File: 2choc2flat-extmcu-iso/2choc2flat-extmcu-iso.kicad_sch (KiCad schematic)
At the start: 136 parts, among them J1 Conn_01x09_Male, J2 Conn_01x05_Male, J3 Conn_01x09_Male, K1 KEYSW, K10 KEYSW, K11 KEYSW, K12 KEYSW, K13 KEYSW, K14 KEYSW, K15-1 KEYSW, K16 KEYSW, K17 KEYSW, K18 KEYSW, K19 KEYSW, K2 KEYSW, K20 KEYSW, K21 KEYSW, K22 KEYSW, K23 KEYSW, K24 KEYSW, K25 KEYSW, K26 KEYSW, K27 KEYSW, K28 KEYSW, K3 KEYSW, K31 KEYSW, K31-1 KEYSW, K32 KEYSW, K33 KEYSW, K34 KEYSW, K35 KEYSW, K36 KEYSW, K37 KEYSW, K38 KEYSW, K39 KEYSW, K4 KEYSW, K40 KEYSW, K41 KEYSW, K42 KEYSW, K43 KEYSW, K44 KEYSW, K46 KEYSW, K48 KEYSW, K49 KEYSW, K5 KEYSW, K50 KEYSW, K51 KEYSW, K52 KEYSW, K53 KEYSW, K54 KEYSW, K55 KEYSW, K56 KEYSW, K57 KEYSW, K58 KEYSW, K59 KEYSW, K6 KEYSW, K61 KEYSW, K62 KEYSW, K63 KEYSW, K67 KEYSW, K7 KEYSW, K71 KEYSW, K72 KEYSW, K73 KEYSW, K74 KEYSW, K8 KEYSW, K9 KEYSW

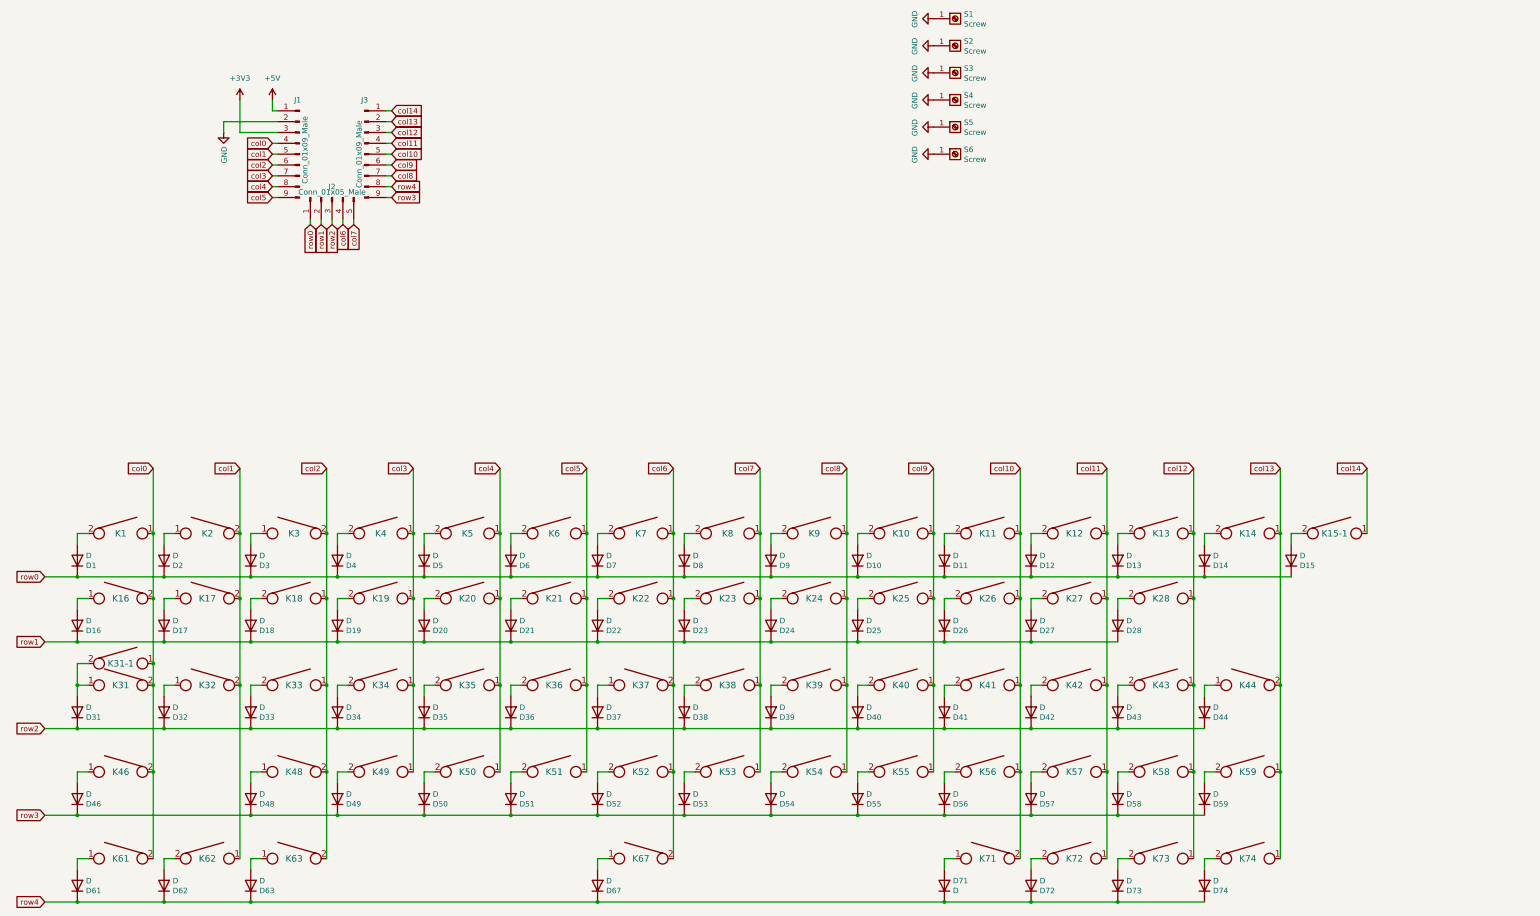
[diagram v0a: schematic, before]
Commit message: make ISO 64 2u left shift layout
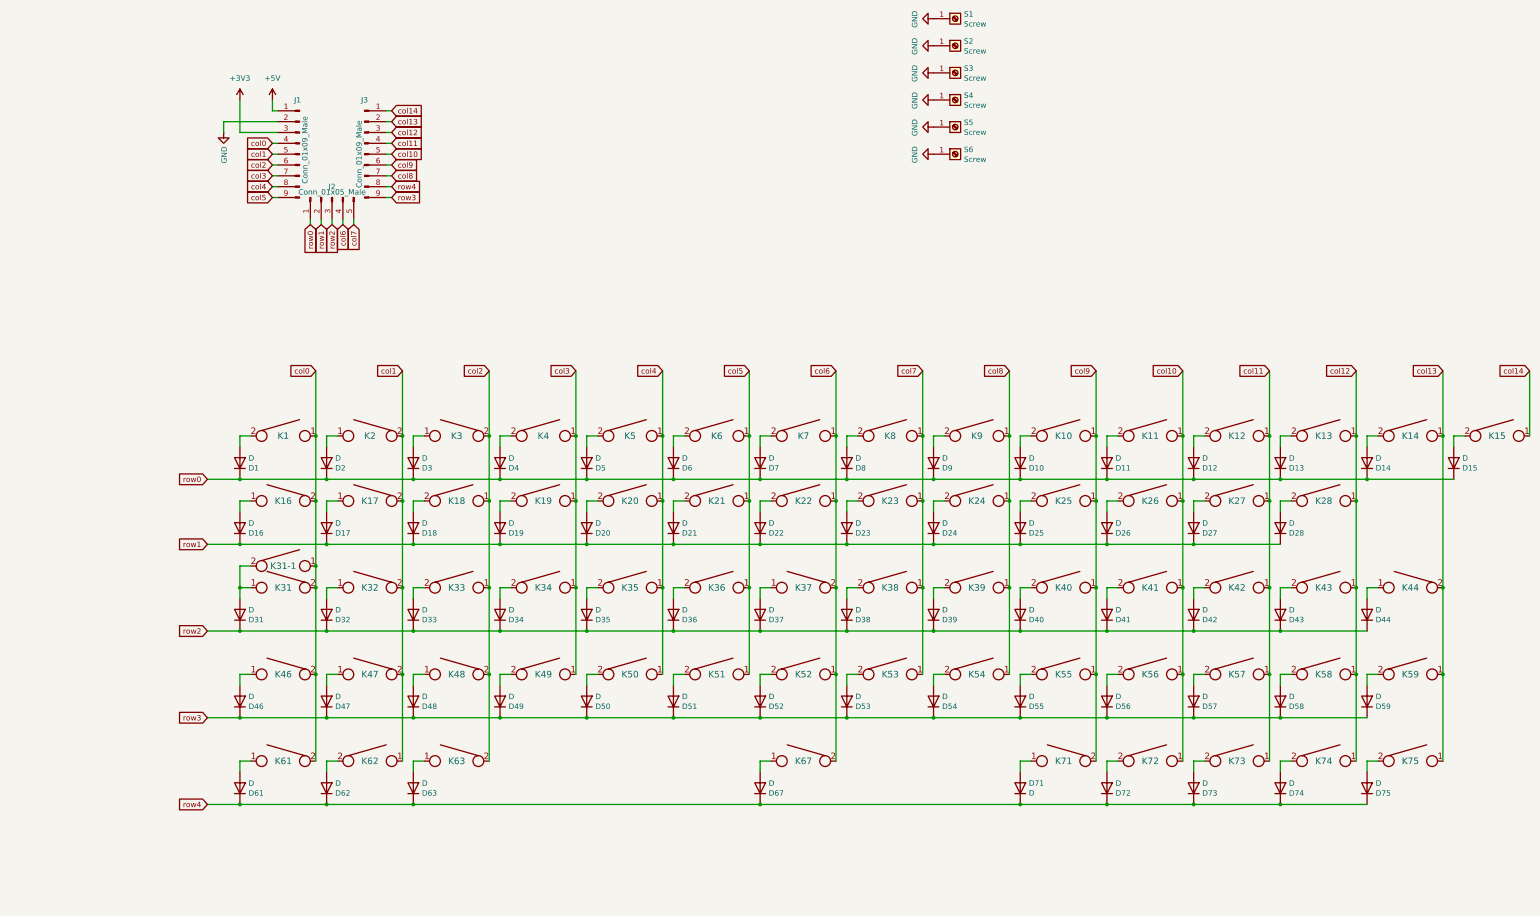
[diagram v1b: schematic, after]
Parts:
- removed K15-1: KEYSW, Switch_Keyboard_Hotswap_Kailh_mine:SW_Hotswap_Kailh_Choc_V2_1.00u, symbol keyboard_parts:KEYSW
- added D47, D75: D, Diode_SMD:D_0805_2012Metric, symbol Device:D
- added K15, K47, K75: KEYSW, Switch_Keyboard_Hotswap_Kailh_mine:SW_Hotswap_Kailh_Choc_V2_1.00u, symbol keyboard_parts:KEYSW
- K46: footprint Switch_Keyboard_Hotswap_Kailh_mine:SW_Hotswap_Kailh_Choc_V2_2.25u_90deg_Gateron_LP_Stabs -> Switch_Keyboard_Hotswap_Kailh_mine:SW_Hotswap_Kailh_Choc_V2_2.00u_90deg_Gateron_LP_Stabs
- K58: footprint Switch_Keyboard_Hotswap_Kailh_mine:SW_Hotswap_Kailh_Choc_V2_1.75u -> Switch_Keyboard_Hotswap_Kailh_mine:SW_Hotswap_Kailh_Choc_V2_1.00u
- K71, K72, K73, K74: footprint Switch_Keyboard_Hotswap_Kailh_mine:SW_Hotswap_Kailh_Choc_V2_1.25u -> Switch_Keyboard_Hotswap_Kailh_mine:SW_Hotswap_Kailh_Choc_V2_1.00u
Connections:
- net col1: now also K47.2
- net col10: now also K72.1; no longer K71.2
- net col11: now also K73.1; no longer K72.1
- net col12: now also K74.1; no longer K73.1
- net col13: now also K75.1; no longer K74.1
- net col14: now also K15.1
- net col9: now also K71.2
- net row3: now also D47.1 (K)
- net row4: now also D75.1 (K)
- net at D15.2 (A): now also K15.2
- new net: D75.2 (A), K75.2
- new net: D47.2 (A), K47.1
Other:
- moved on the sheet: D1, D10, D11, D12, D13, D14, D16, D17, D18, D19, D2, D20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

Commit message: rejigger stabs to work with plates
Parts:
- K67: footprint Switch_Keyboard_Hotswap_Kailh_mine:SW_Hotswap_Kailh_Choc_V2_6.25u_LP_Gateron_Stabs -> Switch_Keyboard_Hotswap_Kailh_mine:SW_Hotswap_Kailh_Choc_V2_6.25u
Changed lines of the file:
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@@
   (junction (at 125.73 158.75) (diameter 0) (color 0 0 0 0)
   )
-  (junction (at 207.01 179.07) (diameter 0) (color 0 0 0 0)
-  )
   (junction (at 85.09 138.43) (diameter 0) (color 0 0 0 0)
   )
@@
   (junction (at 308.61 123.19) (diameter 0) (color 0 0 0 0)
   )
+  (junction (at 207.01 179.07) (diameter 0) (color 0 0 0 0)
+  )
   (junction (at 107.95 133.35) (diameter 0) (color 0 0 0 0)
   )
@@
     (stroke (width 0) (type default) (color 0 0 0 0))
   )
+  (wire (pts (xy 207.01 179.07) (xy 207.01 199.39))
+    (stroke (width 0) (type default) (color 0 0 0 0))
+  )
   (wire (pts (xy 85.09 123.19) (xy 85.09 138.43))
     (stroke (width 0) (type default) (color 0 0 0 0))
@@
     (stroke (width 0) (type default) (color 0 0 0 0))
   )
+  (wire (pts (xy 189.23 199.39) (xy 189.23 201.93))
+    (stroke (width 0) (type default) (color 0 0 0 0))
+  )
   (wire (pts (xy 148.59 140.97) (xy 148.59 138.43))
     (stroke (width 0) (type default) (color 0 0 0 0))
@@
     (stroke (width 0) (type default) (color 0 0 0 0))
   )
+  (wire (pts (xy 191.77 199.39) (xy 189.23 199.39))
+    (stroke (width 0) (type default) (color 0 0 0 0))
+  )
   (wire (pts (xy 351.79 125.73) (xy 351.79 123.19))
     (stroke (width 0) (type default) (color 0 0 0 0))
@@
     (stroke (width 0) (type default) (color 0 0 0 0))
   )
-  (wire (pts (xy 189.23 199.39) (xy 191.77 199.39))
-    (stroke (width 0) (type default) (color 0 0 0 0))
-  )
   (wire (pts (xy 128.27 161.29) (xy 128.27 158.75))
     (stroke (width 0) (type default) (color 0 0 0 0))
@@
     (stroke (width 0) (type default) (color 0 0 0 0))
   )
-  (wire (pts (xy 189.23 201.93) (xy 189.23 199.39))
-    (stroke (width 0) (type default) (color 0 0 0 0))
-  )
   (wire (pts (xy 189.23 148.59) (xy 209.55 148.59))
     (stroke (width 0) (type default) (color 0 0 0 0))
@@
     (stroke (width 0) (type default) (color 0 0 0 0))
   )
-  (wire (pts (xy 207.01 179.07) (xy 207.01 199.39))
-    (stroke (width 0) (type default) (color 0 0 0 0))
-  )
   (wire (pts (xy 166.37 179.07) (xy 166.37 158.75))
     (stroke (width 0) (type default) (color 0 0 0 0))
@@
       (effects (font (size 1.524 1.524)) hide)
     )
-    (property "Footprint" "Switch_Keyboard_Hotswap_Kailh_mine:SW_Hotswap_Kailh_Choc_V2_6.25u_LP_Gateron_Stabs" (id 2) (at 199.39 199.39 0)
+    (property "Footprint" "Switch_Keyboard_Hotswap_Kailh_mine:SW_Hotswap_Kailh_Choc_V2_6.25u" (id 2) (at 199.39 199.39 0)
       (effects (font (size 1.524 1.524)) hide)
     )
@@
     )
     (path "/00000000-0000-0000-0000-00005c555e38"
-      (reference "K67") (unit 1) (value "KEYSW") (footprint "Switch_Keyboard_Hotswap_Kailh_mine:SW_Hotswap_Kailh_Choc_V2_6.25u_LP_Gateron_Stabs")
+      (reference "K67") (unit 1) (value "KEYSW") (footprint "Switch_Keyboard_Hotswap_Kailh_mine:SW_Hotswap_Kailh_Choc_V2_6.25u")
     )
     (path "/00000000-0000-0000-0000-00005cb7e685"

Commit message: relayout using MCU with FFC USB
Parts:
- added LD1: LED, LED_SMD:LED_1206_3216Metric_ReverseMount_Hole1.8x2.4mm, symbol Device:LED
- added R1: R_Small_US, Resistor_SMD:R_0603_1608Metric, symbol Device:R_Small_US
- D1, D10, D11, D12, D13, D14, D15, D16, D17, D18, D19, D2, D20, D21, D22, D23, D24, D25, D26, D27, D28, D3, D32, D33, D34, D35, D36, D37, D38, D39, D4, D40, D41, D42, D43, D44, D46, D47, D48, D49, D5, D50, D51, D52, D53, D54, D55, D56, D57, D58, D59, D6, D61, D62, D63, D67, D7, D71, D72, D73, D74, D75, D8, D9: footprint Diode_SMD:D_0805_2012Metric -> Diode_SMD:D_SOD-323_HandSoldering
- D29: renamed from D31; footprint Diode_SMD:D_0805_2012Metric -> Diode_SMD:D_SOD-323_HandSoldering
- K8: footprint Switch_Keyboard_Kailh_mine:SW_Kailh_Choc_V2_1.00u -> Switch_Keyboard_Hotswap_Kailh_mine:SW_Hotswap_Kailh_Choc_V2_1.00u
- renumbered K31 to K29, K31-1 to K29-1, K32 to K30, K33 to K31, K34 to K32, K35 to K33, K36 to K34, K37 to K35
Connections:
- net +3V3: now also J3.3 (Pin_3); no longer J1.3 (Pin_3)
- net +5V: now also J3.1 (Pin_1); no longer J1.1 (Pin_1)
- net GND: now also J3.2 (Pin_2), LD1.1 (K); no longer J1.2 (Pin_2)
- net col0: now also J3.4 (Pin_4), K16.1, K46.1, K61.1; no longer J1.4 (Pin_4), K16.2, K46.2, K61.2
- net col1: now also J3.5 (Pin_5), K17.1, K2.1, K30.1, K47.1; no longer J1.5 (Pin_5), K17.2, K2.2, K30.2, K47.2
- net col10: now also J1.5 (Pin_5); no longer J3.5 (Pin_5)
- net col11: now also J1.4 (Pin_4); no longer J3.4 (Pin_4)
- net col12: now also J1.3 (Pin_3); no longer J3.3 (Pin_3)
- net col13: now also J1.2 (Pin_2), K15.1; no longer J3.2 (Pin_2)
- net col14: now also J1.1 (Pin_1), R1.1; no longer J3.1 (Pin_1), K15.1
- net col2: now also J3.6 (Pin_6), K3.1, K48.1, K63.1; no longer J1.6 (Pin_6), K3.2, K48.2, K63.2
- net col3: now also J3.7 (Pin_7); no longer J1.7 (Pin_7)
- net col4: now also J3.8 (Pin_8); no longer J1.8 (Pin_8)
- net col5: now also J3.9 (Pin_9); no longer J1.9 (Pin_9)
- net col6: now also J1.9 (Pin_9), K35.1, K67.1; no longer J2.4 (Pin_4), K35.2, K67.2
- net col7: now also J1.8 (Pin_8); no longer J2.5 (Pin_5)
- net col8: now also J1.7 (Pin_7); no longer J3.7 (Pin_7)
- net col9: now also J1.6 (Pin_6), K71.1; no longer J3.6 (Pin_6), K71.2
- net row0: now also J2.5 (Pin_5); no longer D15.1 (K), J2.1 (Pin_1)
- net row1: now also D15.1 (K), J2.4 (Pin_4); no longer J2.2 (Pin_2)
- net row3: now also J2.2 (Pin_2); no longer J3.9 (Pin_9)
- net row4: now also J2.1 (Pin_1); no longer J3.8 (Pin_8)
- net at D2.2 (A): now also K2.2; no longer K2.1
- net at D3.2 (A): now also K3.2; no longer K3.1
- net at D16.2 (A): now also K16.2; no longer K16.1
- net at D17.2 (A): now also K17.2; no longer K17.1
- net at D32.2 (A): now also K30.2; no longer K30.1
- net at D37.2 (A): now also K35.2; no longer K35.1
- net at D46.2 (A): now also K46.2; no longer K46.1
- net at D48.2 (A): now also K48.2; no longer K48.1
- net at D61.2 (A): now also K61.2; no longer K61.1
- net at D63.2 (A): now also K63.2; no longer K63.1
- net at D67.2 (A): now also K67.2; no longer K67.1
- net at D71.2 (A): now also K71.2; no longer K71.1
- net at D47.2 (A): now also K47.2; no longer K47.1
- new net: LD1.2 (A), R1.2
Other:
- moved on the sheet: D15, K15

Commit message: wip renaming stuff
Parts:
- renumbered D32 to D30, D33 to D31, D34 to D32, D35 to D33, D36 to D34, D37 to D35, D38 to D36, D39 to D37, D40 to D38, D41 to D39, D42 to D40, D43 to D41, D44 to D42, K38 to K36, K39 to K37, K40 to K38, K41 to K39, K42 to K40, K43 to K41, K44 to K42

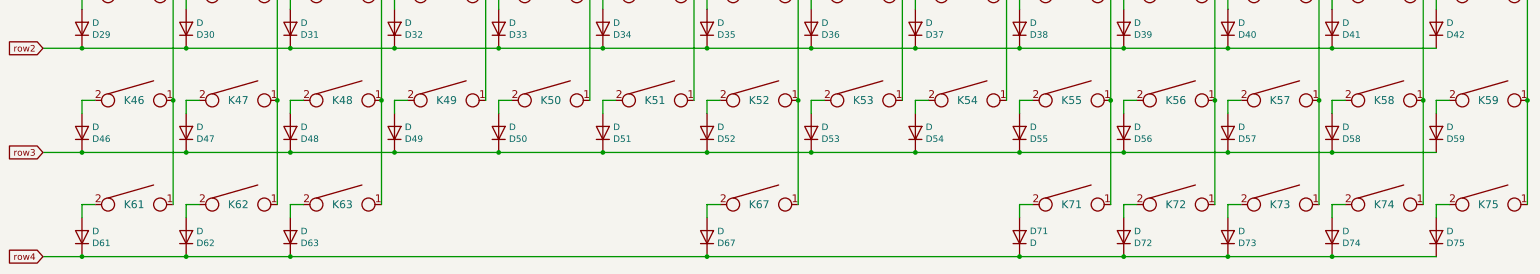
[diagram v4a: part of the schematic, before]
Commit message: rerouted, capslock light
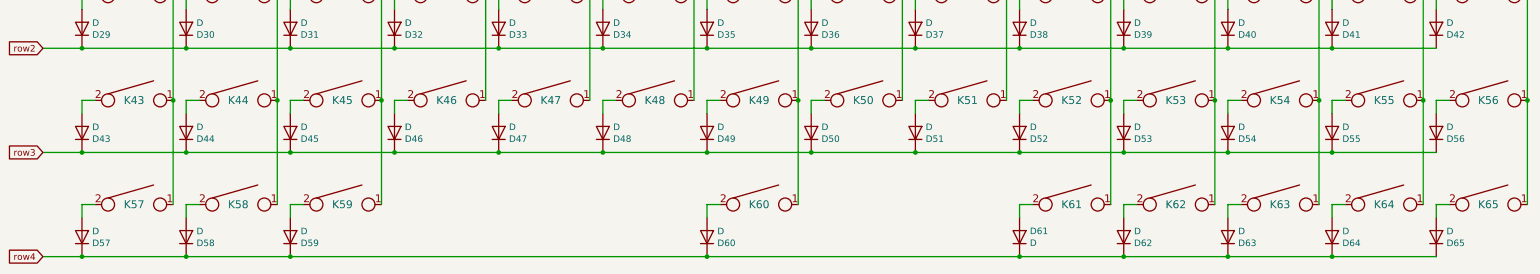
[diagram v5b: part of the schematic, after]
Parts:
- renumbered D46 to D43, D47 to D44, D48 to D45, D49 to D46, D50 to D47, D51 to D48, D52 to D49, D53 to D50, D54 to D51, D55 to D52, D56 to D53, D57 to D54, D58 to D55, D59 to D56, D61 to D57, D62 to D58, D63 to D59, D67 to D60, D71 to D61, D72 to D62, D73 to D63, D74 to D64, D75 to D65, K46 to K43, K47 to K44, K48 to K45, K49 to K46, K50 to K47, K51 to K48, K52 to K49, K53 to K50, K54 to K51, K55 to K52, K56 to K53, K57 to K54, K58 to K55, K59 to K56, K61 to K57, K62 to K58, K63 to K59, K67 to K60, K71 to K61, K72 to K62, K73 to K63, K74 to K64, K75 to K65

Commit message: committing for foam SVGs
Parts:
- K42: footprint Switch_Keyboard_Hotswap_Kailh_mine:SW_Hotswap_Kailh_Choc_V2_ISOEnter_Gateron_LP_Stabs -> Switch_Keyboard_Hotswap_Kailh_mine:SW_Hotswap_Kailh_Choc_V2_ISOEnter_West_Gateron_LP_Stabs
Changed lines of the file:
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@@
       (effects (font (size 1.524 1.524)) hide)
     )
-    (property "Footprint" "Switch_Keyboard_Hotswap_Kailh_mine:SW_Hotswap_Kailh_Choc_V2_ISOEnter_Gateron_LP_Stabs" (id 2) (at 341.63 158.75 0)
+    (property "Footprint" "Switch_Keyboard_Hotswap_Kailh_mine:SW_Hotswap_Kailh_Choc_V2_ISOEnter_West_Gateron_LP_Stabs" (id 2) (at 341.63 158.75 0)
       (effects (font (size 1.524 1.524)) hide)
     )
@@
     )
     (path "/00000000-0000-0000-0000-00005c818730"
-      (reference "K42") (unit 1) (value "KEYSW") (footprint "Switch_Keyboard_Hotswap_Kailh_mine:SW_Hotswap_Kailh_Choc_V2_ISOEnter_Gateron_LP_Stabs")
+      (reference "K42") (unit 1) (value "KEYSW") (footprint "Switch_Keyboard_Hotswap_Kailh_mine:SW_Hotswap_Kailh_Choc_V2_ISOEnter_West_Gateron_LP_Stabs")
     )
     (path "/00000000-0000-0000-0000-00005c5435b9"
